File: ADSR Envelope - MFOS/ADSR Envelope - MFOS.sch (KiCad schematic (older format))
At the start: 56 parts, among them J1 Trigger Input, J2 Gate Input, J3 ADSR Out, SW1 Short or Long Times, SW2 Manual Gate, U1 4066, U2 TL082, U3 CD40106, U4 TL084, U5 4001

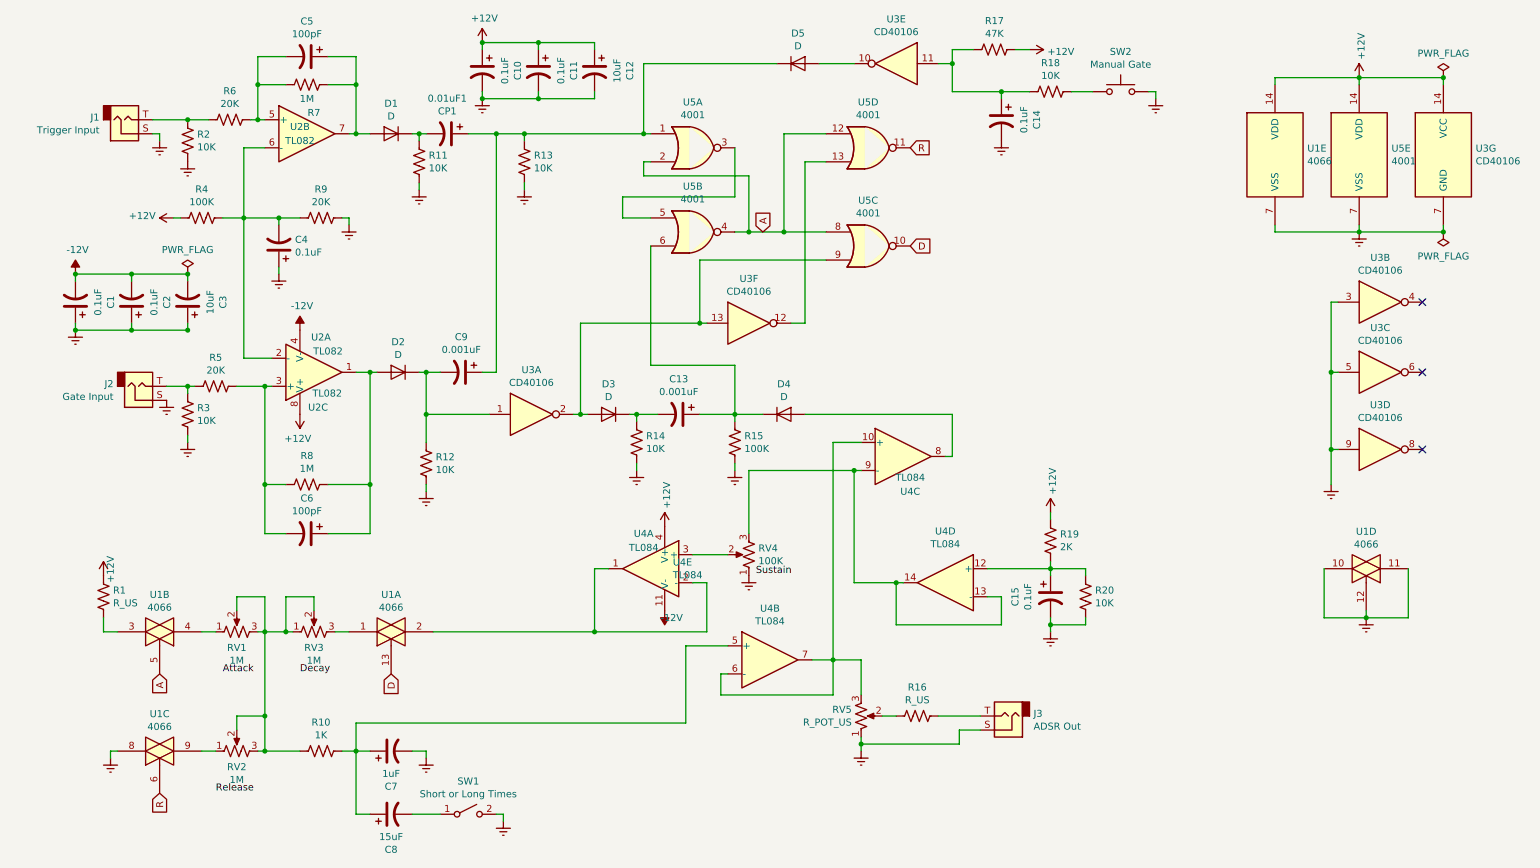
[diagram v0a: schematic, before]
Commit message: checked over schematic and added footprints for all but capacitors
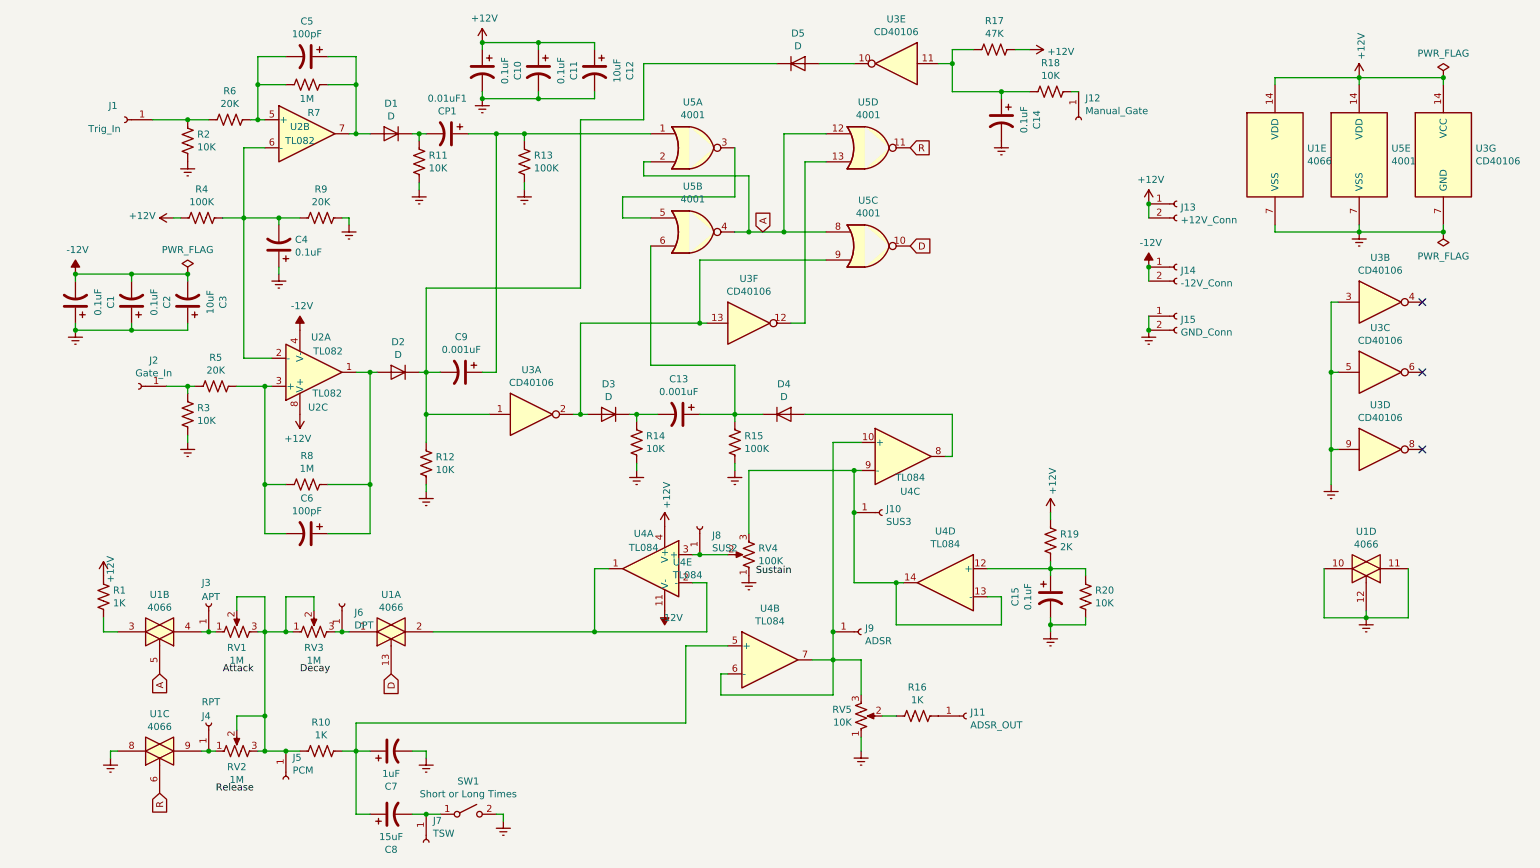
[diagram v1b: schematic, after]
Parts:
- removed J1: Trigger Input, symbol Connector:AudioJack2
- removed J2: Gate Input, symbol Connector:AudioJack2
- removed J3: ADSR Out, symbol Connector:AudioJack2
- removed SW2: Manual Gate, symbol Switch:SW_Push
- added J1: Trig_In, Connector_Wire:SolderWirePad_1x01_Drill1mm, symbol Connector:Conn_01x01_Female
- added J10: SUS3, Connector_Wire:SolderWirePad_1x01_Drill1mm, symbol Connector:Conn_01x01_Female
- added J11: ADSR_OUT, Connector_Wire:SolderWirePad_1x01_Drill1mm, symbol Connector:Conn_01x01_Female
- added J12: Manual_Gate, Connector_Wire:SolderWirePad_1x01_Drill1mm, symbol Connector:Conn_01x01_Female
- added J13: +12V_Conn, Connector_Wire:SolderWirePad_1x02_P3.81mm_Drill1mm, symbol Connector:Conn_01x02_Female
- added J14: -12V_Conn, Connector_Wire:SolderWirePad_1x02_P3.81mm_Drill1mm, symbol Connector:Conn_01x02_Female
- added J15: GND_Conn, Connector_Wire:SolderWirePad_1x02_P3.81mm_Drill1mm, symbol Connector:Conn_01x02_Female
- added J2: Gate_In, Connector_Wire:SolderWirePad_1x01_Drill1mm, symbol Connector:Conn_01x01_Female
- added J3: APT, Connector_Wire:SolderWirePad_1x01_Drill1mm, symbol Connector:Conn_01x01_Female
- added J4: RPT, Connector_Wire:SolderWirePad_1x01_Drill1mm, symbol Connector:Conn_01x01_Female
- added J5: PCM, Connector_Wire:SolderWirePad_1x01_Drill1mm, symbol Connector:Conn_01x01_Female
- added J6: DPT, Connector_Wire:SolderWirePad_1x01_Drill1mm, symbol Connector:Conn_01x01_Female
- added J7: TSW, Connector_Wire:SolderWirePad_1x01_Drill1mm, symbol Connector:Conn_01x01_Female
- added J8: SUS2, Connector_Wire:SolderWirePad_1x01_Drill1mm, symbol Connector:Conn_01x01_Female
- added J9: ADSR, Connector_Wire:SolderWirePad_1x01_Drill1mm, symbol Connector:Conn_01x01_Female
- D1, D2, D3, D4, D5: footprint (none) -> Diode_THT:D_T-1_P5.08mm_Horizontal
- R1, R16: value R_US -> 1K; footprint (none) -> Resistor_THT:R_Axial_DIN0207_L6.3mm_D2.5mm_P7.62mm_Horizontal
- R10, R11, R12, R14, R15, R17, R18, R19, R2, R20, R3, R4, R5, R6, R7, R8, R9: footprint (none) -> Resistor_THT:R_Axial_DIN0207_L6.3mm_D2.5mm_P7.62mm_Horizontal
- R13: value 10K -> 100K; footprint (none) -> Resistor_THT:R_Axial_DIN0207_L6.3mm_D2.5mm_P7.62mm_Horizontal
- RV5: value R_POT_US -> 10K
- U1, U3, U4, U5: footprint (none) -> Package_DIP:DIP-14_W7.62mm_Socket
- U2: footprint (none) -> Package_DIP:DIP-8_W7.62mm_Socket
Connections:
- net +12V: now also J13.1 (Pin_1), J13.2 (Pin_2)
- net -12V: now also J14.1 (Pin_1), J14.2 (Pin_2)
- net Earth: now also J15.1 (Pin_1), J15.2 (Pin_2)
- net at R2.1, R6.2: now also J1.1 (Pin_1)
- net at 0.01uF1.1, C9.1, R13.2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: no longer D5.1 (K)
- net at C9.2, D2.1 (K), R12.1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: now also D5.1 (K)
- net at R3.1, R5.2: now also J2.1 (Pin_1)
- net at RV4.2, U4.3 (+): now also J8.1 (Pin_1)
- net at RV5.3, U4.10 (+), U4.6 (-)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: now also J9.1 (Pin_1)
- net at RV4.3, U4.13 (-), U4.14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: now also J10.1 (Pin_1)
- net at R18.1: now also J12.1 (Pin_1)
- net at RV1.1, U1.4: now also J3.1 (Pin_1)
- net at R10.2, RV1.2, RV1.3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: now also J5.1 (Pin_1)
- net at R16.1: now also J11.1 (Pin_1)
- net at RV3.3, U1.1: now also J6.1 (Pin_1)
- net at RV2.1, U1.9: now also J4.1 (Pin_1)
- net at C8.2, SW1.1 (A): now also J7.1 (Pin_1)

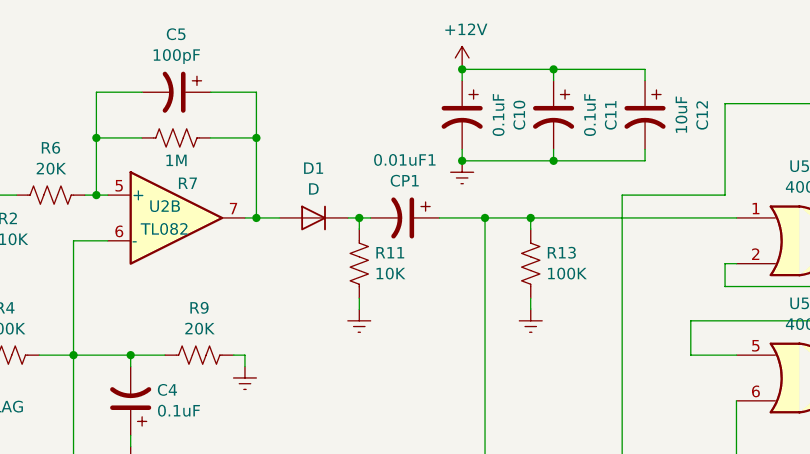
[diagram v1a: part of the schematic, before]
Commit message: assigned footprints
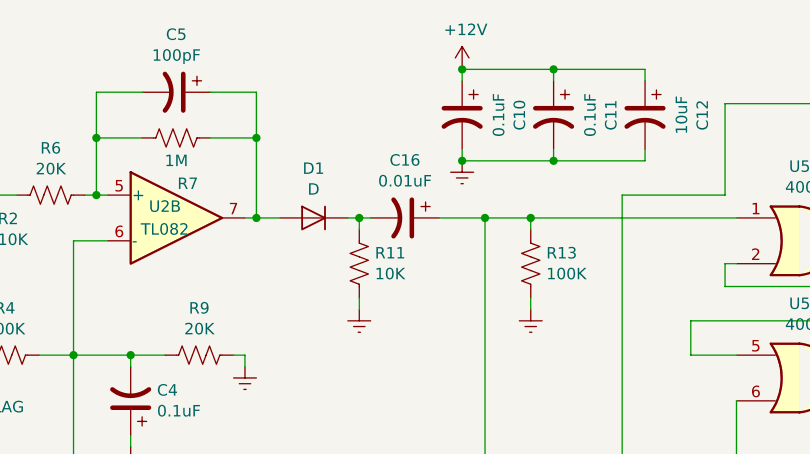
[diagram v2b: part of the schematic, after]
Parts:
- C1, C10, C11, C13, C14, C15, C2, C4, C5, C6, C9: footprint (none) -> Capacitor_THT:C_Rect_L7.0mm_W2.5mm_P5.00mm
- C12, C3, C7: footprint (none) -> Capacitor_THT:CP_Radial_D5.0mm_P2.50mm
- C16: renamed from 0.01uF1; value CP1 -> 0.01uF; footprint (none) -> Capacitor_THT:C_Rect_L7.0mm_W2.5mm_P5.00mm
- C8: footprint (none) -> Capacitor_THT:CP_Radial_D8.0mm_P2.50mm
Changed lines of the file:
@@
 F 0 "C5" V 2198 800 50  0000 C CNN
 F 1 "100pF" V 2289 800 50  0000 C CNN
-F 2 "" H 2450 800 50  0001 C CNN
+F 2 "Capacitor_THT:C_Rect_L7.0mm_W2.5mm_P5.00mm" H 2450 800 50  0001 C CNN
 F 3 "~" H 2450 800 50  0001 C CNN
 	1    2450 800
@@
 F 0 "C4" H 2135 2104 50  0000 R CNN
 F 1 "0.1uF" H 2135 2195 50  0000 R CNN
-F 2 "" H 2250 2150 50  0001 C CNN
+F 2 "Capacitor_THT:C_Rect_L7.0mm_W2.5mm_P5.00mm" H 2250 2150 50  0001 C CNN
 F 3 "~" H 2250 2150 50  0001 C CNN
 	1    2250 2150
@@
 $EndComp
 $Comp
-L Device:CP1 0.01uF1
+L Device:CP1 C16
 U 1 1 5FD5A6BB
 P 3450 1350
-F 0 "0.01uF1" V 3198 1350 50  0000 C CNN
-F 1 "CP1" V 3289 1350 50  0000 C CNN
-F 2 "" H 3450 1350 50  0001 C CNN
+F 0 "C16" V 3198 1350 50  0000 C CNN
+F 1 "0.01uF" V 3289 1350 50  0000 C CNN
+F 2 "Capacitor_THT:C_Rect_L7.0mm_W2.5mm_P5.00mm" H 3450 1350 50  0001 C CNN
 F 3 "~" H 3450 1350 50  0001 C CNN
 	1    3450 1350
@@
 F 0 "C9" V 3298 3050 50  0000 C CNN
 F 1 "0.001uF" V 3389 3050 50  0000 C CNN
-F 2 "" H 3550 3050 50  0001 C CNN
+F 2 "Capacitor_THT:C_Rect_L7.0mm_W2.5mm_P5.00mm" H 3550 3050 50  0001 C CNN
 F 3 "~" H 3550 3050 50  0001 C CNN
 	1    3550 3050
@@
 F 0 "C6" V 2198 4200 50  0000 C CNN
 F 1 "100pF" V 2289 4200 50  0000 C CNN
-F 2 "" H 2450 4200 50  0001 C CNN
+F 2 "Capacitor_THT:C_Rect_L7.0mm_W2.5mm_P5.00mm" H 2450 4200 50  0001 C CNN
 F 3 "~" H 2450 4200 50  0001 C CNN
 	1    2450 4200
@@
 F 0 "C1" V 548 2550 50  0000 C CNN
 F 1 "0.1uF" V 639 2550 50  0000 C CNN
-F 2 "" H 800 2550 50  0001 C CNN
+F 2 "Capacitor_THT:C_Rect_L7.0mm_W2.5mm_P5.00mm" H 800 2550 50  0001 C CNN
 F 3 "~" H 800 2550 50  0001 C CNN
 	1    800  2550
@@
 F 0 "C2" V 948 2550 50  0000 C CNN
 F 1 "0.1uF" V 1039 2550 50  0000 C CNN
-F 2 "" H 1200 2550 50  0001 C CNN
+F 2 "Capacitor_THT:C_Rect_L7.0mm_W2.5mm_P5.00mm" H 1200 2550 50  0001 C CNN
 F 3 "~" H 1200 2550 50  0001 C CNN
 	1    1200 2550
@@
 F 0 "C3" V 1348 2550 50  0000 C CNN
 F 1 "10uF" V 1439 2550 50  0000 C CNN
-F 2 "" H 1600 2550 50  0001 C CNN
+F 2 "Capacitor_THT:CP_Radial_D5.0mm_P2.50mm" H 1600 2550 50  0001 C CNN
 F 3 "~" H 1600 2550 50  0001 C CNN
 	1    1600 2550
@@
 F 0 "C10" V 3448 900 50  0000 C CNN
 F 1 "0.1uF" V 3539 900 50  0000 C CNN
-F 2 "" H 3700 900 50  0001 C CNN
+F 2 "Capacitor_THT:C_Rect_L7.0mm_W2.5mm_P5.00mm" H 3700 900 50  0001 C CNN
 F 3 "~" H 3700 900 50  0001 C CNN
 	1    3700 900
@@
 F 0 "C11" V 3848 900 50  0000 C CNN
 F 1 "0.1uF" V 3939 900 50  0000 C CNN
-F 2 "" H 4100 900 50  0001 C CNN
+F 2 "Capacitor_THT:C_Rect_L7.0mm_W2.5mm_P5.00mm" H 4100 900 50  0001 C CNN
 F 3 "~" H 4100 900 50  0001 C CNN
 	1    4100 900
@@
 F 0 "C12" V 4248 900 50  0000 C CNN
 F 1 "10uF" V 4339 900 50  0000 C CNN
-F 2 "" H 4500 900 50  0001 C CNN
+F 2 "Capacitor_THT:CP_Radial_D5.0mm_P2.50mm" H 4500 900 50  0001 C CNN
 F 3 "~" H 4500 900 50  0001 C CNN
 	1    4500 900
@@
 F 0 "C13" V 4848 3350 50  0000 C CNN
 F 1 "0.001uF" V 4939 3350 50  0000 C CNN
-F 2 "" H 5100 3350 50  0001 C CNN
+F 2 "Capacitor_THT:C_Rect_L7.0mm_W2.5mm_P5.00mm" H 5100 3350 50  0001 C CNN
 F 3 "~" H 5100 3350 50  0001 C CNN
 	1    5100 3350
@@
 F 0 "C14" V 7148 1250 50  0000 C CNN
 F 1 "0.1uF" V 7239 1250 50  0000 C CNN
-F 2 "" H 7400 1250 50  0001 C CNN
+F 2 "Capacitor_THT:C_Rect_L7.0mm_W2.5mm_P5.00mm" H 7400 1250 50  0001 C CNN
 F 3 "~" H 7400 1250 50  0001 C CNN
 	1    7400 1250
@@
 F 0 "C15" V 7498 4650 50  0000 C CNN
 F 1 "0.1uF" V 7589 4650 50  0000 C CNN
-F 2 "" H 7750 4650 50  0001 C CNN
+F 2 "Capacitor_THT:C_Rect_L7.0mm_W2.5mm_P5.00mm" H 7750 4650 50  0001 C CNN
 F 3 "~" H 7750 4650 50  0001 C CNN
 	1    7750 4650
@@
 F 0 "C7" V 2798 5750 50  0000 C CNN
 F 1 "1uF" V 2889 5750 50  0000 C CNN
-F 2 "" H 3050 5750 50  0001 C CNN
+F 2 "Capacitor_THT:CP_Radial_D5.0mm_P2.50mm" H 3050 5750 50  0001 C CNN
 F 3 "~" H 3050 5750 50  0001 C CNN
 	1    3050 5750
@@
 F 0 "C8" V 2798 6200 50  0000 C CNN
 F 1 "15uF" V 2889 6200 50  0000 C CNN
-F 2 "" H 3050 6200 50  0001 C CNN
+F 2 "Capacitor_THT:CP_Radial_D8.0mm_P2.50mm" H 3050 6200 50  0001 C CNN
 F 3 "~" H 3050 6200 50  0001 C CNN
 	1    3050 6200

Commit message: layout passes drc
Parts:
- C8: footprint Capacitor_THT:CP_Radial_D8.0mm_P2.50mm -> Capacitor_THT:CP_Radial_D5.0mm_P2.50mm
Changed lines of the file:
@@
 F 0 "C8" V 2798 6200 50  0000 C CNN
 F 1 "15uF" V 2889 6200 50  0000 C CNN
-F 2 "Capacitor_THT:CP_Radial_D8.0mm_P2.50mm" H 3050 6200 50  0001 C CNN
+F 2 "Capacitor_THT:CP_Radial_D5.0mm_P2.50mm" H 3050 6200 50  0001 C CNN
 F 3 "~" H 3050 6200 50  0001 C CNN
 	1    3050 6200
